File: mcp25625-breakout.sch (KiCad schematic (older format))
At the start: 7 parts, among them J1 Conn_01x10, SW1 SW_Slide_with_cover, U1 MCP25625-x-SS, Y1 Resonator

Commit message: Add reset pad and 16MHz mems as rev2021.07
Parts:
- removed Y1: Resonator, my-kicad-footprints:Resonator_SMD_Murata_CSTxExxV-3Pin_3.0x1.1mm_narrow, symbol Device:Resonator
- added C3: 0.1uf, Capacitor_SMD:C_0402_1005Metric, symbol Device:C
- added C4: 1uf, Capacitor_SMD:C_0402_1005Metric, symbol Device:C
- added C5: 22pf, Capacitor_SMD:C_0402_1005Metric, symbol Device:C
- added R2: 10k, Resistor_SMD:R_0402_1005Metric, symbol Device:R
- added U2: NJM2866F33, Package_TO_SOT_SMD:SOT-23-5, symbol my-kicad-symbols:NJM2866F33
- added U3: SiT2001B-MEMS-Clock-Generator, Package_TO_SOT_SMD:SOT-23-5, symbol my-kicad-symbols:SiT2001B-MEMS-Clock-Generator
- J1: value Conn_01x10 -> Conn_01x11; footprint my-kicad-footprints:PinHeader_1x10_P2.54mm_Vertical_witout_silk -> my-kicad-footprints:PinHeader_1x11_P2.54mm_Vertical_witout_silk; symbol Connector_Generic:Conn_01x10 -> Connector_Generic:Conn_01x11
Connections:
- net CANH: now also J1.10 (Pin_10); no longer J1.9 (Pin_9)
- net CANL: now also J1.11 (Pin_11); no longer J1.10 (Pin_10)
- net GND: now also J1.9 (Pin_9), C3.2, C4.2, C5.2, U2.2 (GND), U3.1 (GND); no longer J1.8 (Pin_8)
- net V_DDA: now also J1.8 (Pin_8); no longer J1.7 (Pin_7)
- net V_IO: now also J1.7 (Pin_7), C3.1, R2.1, U2.1 (VIN); no longer J1.6 (Pin_6)
- net RESET: now reaches U1.18 (~RESET)
- net RESET: now also J1.6 (Pin_6)
- net 16MHz: now reaches U1.9 (OSC1)
- net 16MHz: now also C5.1, U3.5 (OUT)
- new net: R2.2, U2.3 (CTL)
- new net +3V3: C4.1, U2.5 (Vout), U3.4 (VDD)
- no-connect marks 8 -> 10
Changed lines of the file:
@@
 NoConn ~ 4500 3600
 NoConn ~ 4500 3500
-NoConn ~ 4500 3300
-$Comp
-L Device:Resonator Y1
-U 1 1 6096B95F
-P 5850 3850
-F 0 "Y1" V 6150 3700 50  0000 L CNN
-F 1 "Resonator" V 6050 3400 50  0000 L CNN
-F 2 "my-kicad-footprints:Resonator_SMD_Murata_CSTxExxV-3Pin_3.0x1.1mm_narrow" H 5825 3850 50  0001 C CNN
-F 3 "~" H 5825 3850 50  0001 C CNN
-	1    5850 3850
-	0    -1   -1   0
-$EndComp
 $Comp
 L Interface_CAN_LIN:MCP25625-x-SS U1
@@
 $EndComp
 Wire Wire Line
-	5850 3700 5700 3700
-Wire Wire Line
 	5700 4000 5850 4000
-Wire Wire Line
-	6050 3850 6050 4700
-Wire Wire Line
-	6050 4700 5300 4700
 $Comp
 L Device:C C2
@@
 $EndComp
 $Comp
-L power:GND #PWR0103
-U 1 1 6096ED61
-P 4400 2600
-F 0 "#PWR0103" H 4400 2350 50  0001 C CNN
-F 1 "GND" H 4500 2600 50  0000 C CNN
-F 2 "" H 4400 2600 50  0001 C CNN
-F 3 "" H 4400 2600 50  0001 C CNN
-	1    4400 2600
-	-1   0    0    -1
-$EndComp
-Wire Wire Line
-	4400 2600 4500 2600
-$Comp
 L power:GND #PWR0104
 U 1 1 60970825
@@
 Text Label 6100 2950 0    50   ~ 0
 CANL
-Text Label 3100 3600 0    50   ~ 0
+Text Label 3100 3700 0    50   ~ 0
 CANH
-Text Label 3100 3700 0    50   ~ 0
+Text Label 3100 3800 0    50   ~ 0
 CANL
 $Comp
 L power:GND #PWR0105
 U 1 1 60A3EF40
-P 3400 3500
-F 0 "#PWR0105" H 3400 3250 50  0001 C CNN
-F 1 "GND" H 3405 3327 50  0000 C CNN
-F 2 "" H 3400 3500 50  0001 C CNN
-F 3 "" H 3400 3500 50  0001 C CNN
-	1    3400 3500
+P 3500 3600
+F 0 "#PWR0105" H 3500 3350 50  0001 C CNN
+F 1 "GND" H 3600 3600 50  0000 C CNN
+F 2 "" H 3500 3600 50  0001 C CNN
+F 3 "" H 3500 3600 50  0001 C CNN
+	1    3500 3600
 	1    0    0    -1
 $EndComp
@@
 INT
 $Comp
-L Connector_Generic:Conn_01x10 J1
+L Connector_Generic:Conn_01x11 J1
 U 1 1 60A42D68
-P 2900 3200
-F 0 "J1" H 2818 3817 50  0000 C CNN
-F 1 "Conn_01x10" H 2818 3726 50  0000 C CNN
-F 2 "my-kicad-footprints:PinHeader_1x10_P2.54mm_Vertical_witout_silk" H 2900 3200 50  0001 C CNN
-F 3 "~" H 2900 3200 50  0001 C CNN
-	1    2900 3200
-	-1   0    0    -1
-$EndComp
-Wire Wire Line
-	3400 3500 3100 3500
-Text Label 3100 3300 0    50   ~ 0
+P 2900 3300
+F 0 "J1" H 2800 4050 50  0000 C CNN
+F 1 "Conn_01x11" H 2800 3950 50  0000 C CNN
+F 2 "my-kicad-footprints:PinHeader_1x11_P2.54mm_Vertical_witout_silk" H 2900 3300 50  0001 C CNN
+F 3 "~" H 2900 3300 50  0001 C CNN
+	1    2900 3300
+	-1   0    0    -1
+$EndComp
+Text Label 3100 3400 0    50   ~ 0
 V_IO
-Text Label 3100 3400 0    50   ~ 0
+Text Label 3100 3500 0    50   ~ 0
 V_DDA
 Text Label 4550 1800 0    50   ~ 0
@@
 	6250 2400 6450 2400
 NoConn ~ 6450 2600
+$Comp
+L my-kicad-symbols:SiT2001B-MEMS-Clock-Generator U3
+U 1 1 60EA6BF5
+P 8450 4400
+F 0 "U3" H 8600 4750 50  0000 L CNN
+F 1 "SiT2001B-MEMS-Clock-Generator" H 8600 4850 50  0000 L CNN
+F 2 "Package_TO_SOT_SMD:SOT-23-5" H 8450 4400 50  0001 C CNN
+F 3 "" H 8450 4400 50  0001 C CNN
+	1    8450 4400
+	1    0    0    -1
+$EndComp
+NoConn ~ 5700 3700
+Text Label 3100 3300 0    50   ~ 0
+RESET
+Text Label 4500 3300 2    50   ~ 0
+RESET
+$Comp
+L power:GND #PWR0103
+U 1 1 6096ED61
+P 4500 2600
+F 0 "#PWR0103" H 4500 2350 50  0001 C CNN
+F 1 "GND" H 4600 2600 50  0000 C CNN
+F 2 "" H 4500 2600 50  0001 C CNN
+F 3 "" H 4500 2600 50  0001 C CNN
+	1    4500 2600
+	-1   0    0    -1
+$EndComp
+Text Label 9150 4300 0    50   ~ 0
+16MHz
+$Comp
+L Device:C C5
+U 1 1 60EB2EF2
+P 9000 4450
+F 0 "C5" H 9115 4496 50  0000 L CNN
+F 1 "22pf" H 9115 4405 50  0000 L CNN
+F 2 "Capacitor_SMD:C_0402_1005Metric" H 9038 4300 50  0001 C CNN
+F 3 "~" H 9000 4450 50  0001 C CNN
+	1    9000 4450
+	1    0    0    -1
+$EndComp
+Wire Wire Line
+	9150 4300 9000 4300
+Connection ~ 9000 4300
+Wire Wire Line
+	9000 4300 8850 4300
+Text Label 5850 4000 0    50   ~ 0
+16MHz
+$Comp
+L power:GND #PWR0107
+U 1 1 60EB5118
+P 8450 4800
+F 0 "#PWR0107" H 8450 4550 50  0001 C CNN
+F 1 "GND" H 8455 4627 50  0000 C CNN
+F 2 "" H 8450 4800 50  0001 C CNN
+F 3 "" H 8450 4800 50  0001 C CNN
+	1    8450 4800
+	1    0    0    -1
+$EndComp
+Wire Wire Line
+	8450 4800 9000 4800
+Wire Wire Line
+	9000 4800 9000 4600
+Connection ~ 8450 4800
+Wire Wire Line
+	3100 3600 3500 3600
+Text Label 6650 3900 2    50   ~ 0
+V_IO
+NoConn ~ 8050 4400
+$Comp
+L Device:R R2
+U 1 1 60ED09D5
+P 6650 4150
+F 0 "R2" H 6720 4196 50  0000 L CNN
+F 1 "10k" H 6720 4105 50  0000 L CNN
+F 2 "Resistor_SMD:R_0402_1005Metric" V 6580 4150 50  0001 C CNN
+F 3 "~" H 6650 4150 50  0001 C CNN
+	1    6650 4150
+	-1   0    0    -1
+$EndComp
+Wire Wire Line
+	6650 4300 6700 4300
+Wire Wire Line
+	6650 3900 6650 3950
+Wire Wire Line
+	6650 3950 7100 3950
+Wire Wire Line
+	7100 3950 7100 4000
+Connection ~ 6650 3950
+Wire Wire Line
+	6650 3950 6650 4000
+$Comp
+L my-kicad-symbols:NJM2866F33 U2
+U 1 1 60ED38A2
+P 7100 4300
+F 0 "U2" H 7150 4650 50  0000 C CNN
+F 1 "NJM2866F33" H 7350 4550 50  0000 C CNN
+F 2 "Package_TO_SOT_SMD:SOT-23-5" H 7100 4300 50  0001 C CNN
+F 3 "" H 7100 4300 50  0001 C CNN
+	1    7100 4300
+	1    0    0    -1
+$EndComp
+NoConn ~ 7500 4400
+$Comp
+L power:GND #PWR0108
+U 1 1 60ED514C
+P 7100 4600
+F 0 "#PWR0108" H 7100 4350 50  0001 C CNN
+F 1 "GND" H 7105 4427 50  0000 C CNN
+F 2 "" H 7100 4600 50  0001 C CNN
+F 3 "" H 7100 4600 50  0001 C CNN
+	1    7100 4600
+	1    0    0    -1
+$EndComp
+$Comp
+L Device:C C4
+U 1 1 60ED568F
+P 7650 4350
+F 0 "C4" H 7765 4396 50  0000 L CNN
+F 1 "1uf" H 7765 4305 50  0000 L CNN
+F 2 "Capacitor_SMD:C_0402_1005Metric" H 7688 4200 50  0001 C CNN
+F 3 "~" H 7650 4350 50  0001 C CNN
+	1    7650 4350
+	1    0    0    -1
+$EndComp
+$Comp
+L power:+3V3 #PWR0109
+U 1 1 60ED5F23
+P 7650 4100
+F 0 "#PWR0109" H 7650 3950 50  0001 C CNN
+F 1 "+3V3" H 7665 4273 50  0000 C CNN
+F 2 "" H 7650 4100 50  0001 C CNN
+F 3 "" H 7650 4100 50  0001 C CNN
+	1    7650 4100
+	1    0    0    -1
+$EndComp
+Wire Wire Line
+	7650 4100 7650 4200
+Wire Wire Line
+	7650 4200 7500 4200
+Connection ~ 7650 4200
+$Comp
+L power:+3V3 #PWR0110
+U 1 1 60ED69C1
+P 8450 4000
+F 0 "#PWR0110" H 8450 3850 50  0001 C CNN
+F 1 "+3V3" H 8465 4173 50  0000 C CNN
+F 2 "" H 8450 4000 50  0001 C CNN
+F 3 "" H 8450 4000 50  0001 C CNN
+	1    8450 4000
+	1    0    0    -1
+$EndComp
+Wire Wire Line
+	7650 4500 7650 4600
+Wire Wire Line
+	7650 4600 7100 4600
+Connection ~ 7100 4600
+$Comp
+L Device:C C3
+U 1 1 60ED7980
+P 6400 4350
+F 0 "C3" H 6515 4396 50  0000 L CNN
+F 1 "0.1uf" H 6515 4305 50  0000 L CNN
+F 2 "Capacitor_SMD:C_0402_1005Metric" H 6438 4200 50  0001 C CNN
+F 3 "~" H 6400 4350 50  0001 C CNN
+	1    6400 4350
+	-1   0    0    -1
+$EndComp
+Wire Wire Line
+	6400 4200 6400 3950
+Wire Wire Line
+	6400 3950 6650 3950
+Wire Wire Line
+	6400 4500 6400 4600
+Wire Wire Line
+	6400 4600 7100 4600
 $EndSCHEMATC

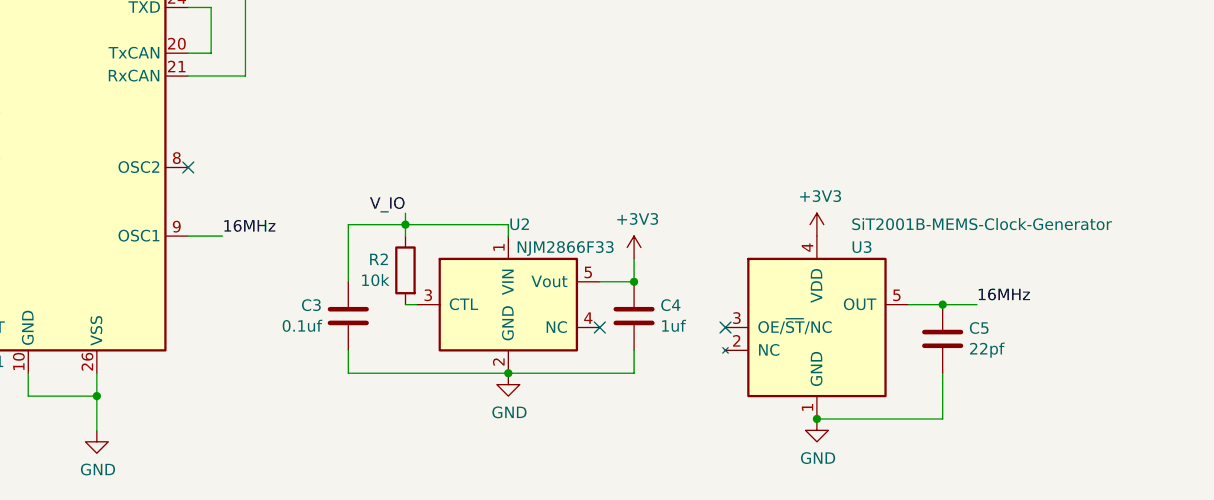
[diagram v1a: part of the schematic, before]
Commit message: Replace rezonator to crystal
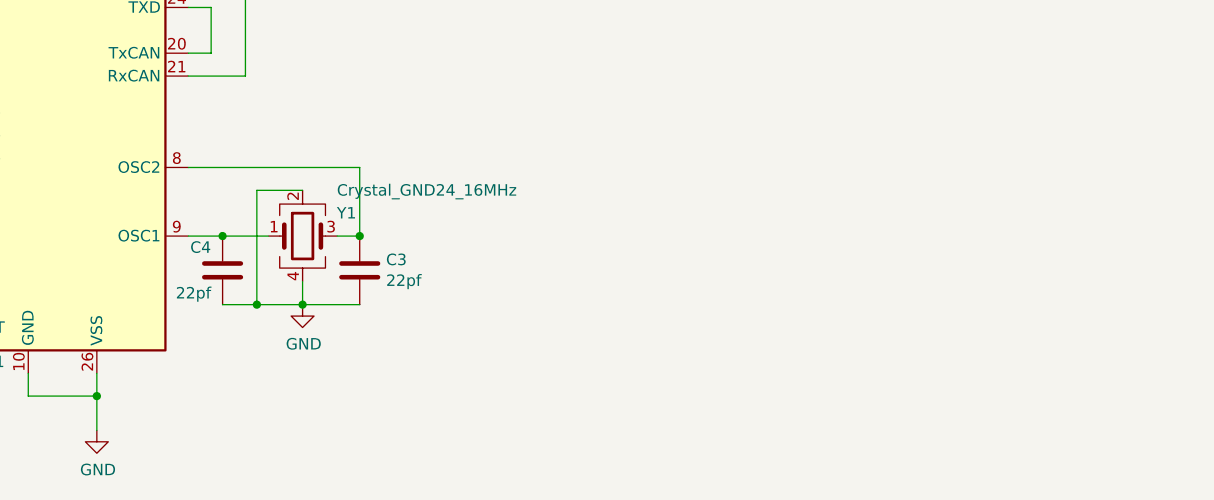
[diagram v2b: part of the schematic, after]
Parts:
- removed C4: 1uf, Capacitor_SMD:C_0402_1005Metric, symbol Device:C
- removed R2: 10k, Resistor_SMD:R_0402_1005Metric, symbol Device:R
- removed U2: NJM2866F33, Package_TO_SOT_SMD:SOT-23-5, symbol my-kicad-symbols:NJM2866F33
- removed U3: SiT2001B-MEMS-Clock-Generator, Package_TO_SOT_SMD:SOT-23-5, symbol my-kicad-symbols:SiT2001B-MEMS-Clock-Generator
- added Y1: Crystal_GND24_16MHz, Crystal:Crystal_SMD_SeikoEpson_FA238-4Pin_3.2x2.5mm_HandSoldering, symbol Device:Crystal_GND24
- C3: value 0.1uf -> 22pf
- renumbered C5 to C4
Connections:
- net GND: now also Y1.2, Y1.4
- net V_IO: no longer C3.1
- net at U1.8 (OSC2): now also C3.1, Y1.3
- net 16MHz: no longer names the net of C4.1, U1.9 (OSC1)
- net 16MHz: now also Y1.1
- no-connect marks 10 -> 7
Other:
- moved on the sheet: C4
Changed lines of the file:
@@
 	1    0    0    -1
 $EndComp
-Wire Wire Line
-	5700 4000 5850 4000
 $Comp
 L Device:C C2
@@
 	6250 2400 6450 2400
 NoConn ~ 6450 2600
-$Comp
-L my-kicad-symbols:SiT2001B-MEMS-Clock-Generator U3
-U 1 1 60EA6BF5
-P 8450 4400
-F 0 "U3" H 8600 4750 50  0000 L CNN
-F 1 "SiT2001B-MEMS-Clock-Generator" H 8600 4850 50  0000 L CNN
-F 2 "Package_TO_SOT_SMD:SOT-23-5" H 8450 4400 50  0001 C CNN
-F 3 "" H 8450 4400 50  0001 C CNN
-	1    8450 4400
-	1    0    0    -1
-$EndComp
-NoConn ~ 5700 3700
 Text Label 3100 3300 0    50   ~ 0
 RESET
@@
 	-1   0    0    -1
 $EndComp
-Text Label 9150 4300 0    50   ~ 0
-16MHz
-$Comp
-L Device:C C5
+$Comp
+L Device:C C4
 U 1 1 60EB2EF2
-P 9000 4450
-F 0 "C5" H 9115 4496 50  0000 L CNN
-F 1 "22pf" H 9115 4405 50  0000 L CNN
-F 2 "Capacitor_SMD:C_0402_1005Metric" H 9038 4300 50  0001 C CNN
-F 3 "~" H 9000 4450 50  0001 C CNN
-	1    9000 4450
-	1    0    0    -1
-$EndComp
-Wire Wire Line
-	9150 4300 9000 4300
-Connection ~ 9000 4300
-Wire Wire Line
-	9000 4300 8850 4300
-Text Label 5850 4000 0    50   ~ 0
-16MHz
+P 5850 4150
+F 0 "C4" H 5900 4250 50  0000 L CNN
+F 1 "22pf" H 5900 4050 50  0000 L CNN
+F 2 "Capacitor_SMD:C_0402_1005Metric" H 5888 4000 50  0001 C CNN
+F 3 "~" H 5850 4150 50  0001 C CNN
+	1    5850 4150
+	-1   0    0    -1
+$EndComp
+Wire Wire Line
+	3100 3600 3500 3600
+$Comp
+L Device:Crystal_GND24 Y1
+U 1 1 61607A20
+P 6200 4000
+F 0 "Y1" H 6350 4100 50  0000 L CNN
+F 1 "Crystal_GND24_16MHz" H 6350 4200 50  0000 L CNN
+F 2 "Crystal:Crystal_SMD_SeikoEpson_FA238-4Pin_3.2x2.5mm_HandSoldering" H 6200 4000 50  0001 C CNN
+F 3 "~" H 6200 4000 50  0001 C CNN
+	1    6200 4000
+	1    0    0    -1
+$EndComp
+$Comp
+L Device:C C3
+U 1 1 61613BC8
+P 6450 4150
+F 0 "C3" H 6565 4196 50  0000 L CNN
+F 1 "22pf" H 6565 4105 50  0000 L CNN
+F 2 "Capacitor_SMD:C_0402_1005Metric" H 6488 4000 50  0001 C CNN
+F 3 "~" H 6450 4150 50  0001 C CNN
+	1    6450 4150
+	1    0    0    -1
+$EndComp
+Wire Wire Line
+	5700 3700 6450 3700
+Wire Wire Line
+	6450 3700 6450 4000
+Wire Wire Line
+	6450 4000 6350 4000
+Connection ~ 6450 4000
+Wire Wire Line
+	5700 4000 5850 4000
 $Comp
 L power:GND #PWR0107
-U 1 1 60EB5118
-P 8450 4800
-F 0 "#PWR0107" H 8450 4550 50  0001 C CNN
-F 1 "GND" H 8455 4627 50  0000 C CNN
-F 2 "" H 8450 4800 50  0001 C CNN
-F 3 "" H 8450 4800 50  0001 C CNN
-	1    8450 4800
-	1    0    0    -1
-$EndComp
-Wire Wire Line
-	8450 4800 9000 4800
-Wire Wire Line
-	9000 4800 9000 4600
-Connection ~ 8450 4800
-Wire Wire Line
-	3100 3600 3500 3600
-Text Label 6650 3900 2    50   ~ 0
-V_IO
-NoConn ~ 8050 4400
-$Comp
-L Device:R R2
-U 1 1 60ED09D5
-P 6650 4150
-F 0 "R2" H 6720 4196 50  0000 L CNN
-F 1 "10k" H 6720 4105 50  0000 L CNN
-F 2 "Resistor_SMD:R_0402_1005Metric" V 6580 4150 50  0001 C CNN
-F 3 "~" H 6650 4150 50  0001 C CNN
-	1    6650 4150
-	-1   0    0    -1
-$EndComp
-Wire Wire Line
-	6650 4300 6700 4300
-Wire Wire Line
-	6650 3900 6650 3950
-Wire Wire Line
-	6650 3950 7100 3950
-Wire Wire Line
-	7100 3950 7100 4000
-Connection ~ 6650 3950
-Wire Wire Line
-	6650 3950 6650 4000
-$Comp
-L my-kicad-symbols:NJM2866F33 U2
-U 1 1 60ED38A2
-P 7100 4300
-F 0 "U2" H 7150 4650 50  0000 C CNN
-F 1 "NJM2866F33" H 7350 4550 50  0000 C CNN
-F 2 "Package_TO_SOT_SMD:SOT-23-5" H 7100 4300 50  0001 C CNN
-F 3 "" H 7100 4300 50  0001 C CNN
-	1    7100 4300
-	1    0    0    -1
-$EndComp
-NoConn ~ 7500 4400
-$Comp
-L power:GND #PWR0108
-U 1 1 60ED514C
-P 7100 4600
-F 0 "#PWR0108" H 7100 4350 50  0001 C CNN
-F 1 "GND" H 7105 4427 50  0000 C CNN
-F 2 "" H 7100 4600 50  0001 C CNN
-F 3 "" H 7100 4600 50  0001 C CNN
-	1    7100 4600
-	1    0    0    -1
-$EndComp
-$Comp
-L Device:C C4
-U 1 1 60ED568F
-P 7650 4350
-F 0 "C4" H 7765 4396 50  0000 L CNN
-F 1 "1uf" H 7765 4305 50  0000 L CNN
-F 2 "Capacitor_SMD:C_0402_1005Metric" H 7688 4200 50  0001 C CNN
-F 3 "~" H 7650 4350 50  0001 C CNN
-	1    7650 4350
-	1    0    0    -1
-$EndComp
-$Comp
-L power:+3V3 #PWR0109
-U 1 1 60ED5F23
-P 7650 4100
-F 0 "#PWR0109" H 7650 3950 50  0001 C CNN
-F 1 "+3V3" H 7665 4273 50  0000 C CNN
-F 2 "" H 7650 4100 50  0001 C CNN
-F 3 "" H 7650 4100 50  0001 C CNN
-	1    7650 4100
-	1    0    0    -1
-$EndComp
-Wire Wire Line
-	7650 4100 7650 4200
-Wire Wire Line
-	7650 4200 7500 4200
-Connection ~ 7650 4200
-$Comp
-L power:+3V3 #PWR0110
-U 1 1 60ED69C1
-P 8450 4000
-F 0 "#PWR0110" H 8450 3850 50  0001 C CNN
-F 1 "+3V3" H 8465 4173 50  0000 C CNN
-F 2 "" H 8450 4000 50  0001 C CNN
-F 3 "" H 8450 4000 50  0001 C CNN
-	1    8450 4000
-	1    0    0    -1
-$EndComp
-Wire Wire Line
-	7650 4500 7650 4600
-Wire Wire Line
-	7650 4600 7100 4600
-Connection ~ 7100 4600
-$Comp
-L Device:C C3
-U 1 1 60ED7980
-P 6400 4350
-F 0 "C3" H 6515 4396 50  0000 L CNN
-F 1 "0.1uf" H 6515 4305 50  0000 L CNN
-F 2 "Capacitor_SMD:C_0402_1005Metric" H 6438 4200 50  0001 C CNN
-F 3 "~" H 6400 4350 50  0001 C CNN
-	1    6400 4350
-	-1   0    0    -1
-$EndComp
-Wire Wire Line
-	6400 4200 6400 3950
-Wire Wire Line
-	6400 3950 6650 3950
-Wire Wire Line
-	6400 4500 6400 4600
-Wire Wire Line
-	6400 4600 7100 4600
+U 1 1 61615DF3
+P 6200 4300
+F 0 "#PWR0107" H 6200 4050 50  0001 C CNN
+F 1 "GND" H 6205 4127 50  0000 C CNN
+F 2 "" H 6200 4300 50  0001 C CNN
+F 3 "" H 6200 4300 50  0001 C CNN
+	1    6200 4300
+	1    0    0    -1
+$EndComp
+Wire Wire Line
+	6450 4300 6200 4300
+Connection ~ 6200 4300
+Wire Wire Line
+	6200 4300 6200 4200
+Connection ~ 5850 4000
+Wire Wire Line
+	5850 4000 6050 4000
+Wire Wire Line
+	5850 4300 6000 4300
+Wire Wire Line
+	6200 3800 6000 3800
+Wire Wire Line
+	6000 3800 6000 4300
+Connection ~ 6000 4300
+Wire Wire Line
+	6000 4300 6200 4300
 $EndSCHEMATC
